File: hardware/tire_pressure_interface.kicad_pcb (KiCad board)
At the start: 4 copper layers, 60.3 x 60.4 mm, 82 parts, among them IC1 TPS54202HDDCR, J3 FTSH-107-01-L-D-K, J4 Conn_02x02_Counter_Clockwise, J5 Micro_SD_Card_Det1, Q1 SI2347DS-T1-GE3, T1 TP_+3V3, T10 TP_+5V, T11 TP_+5V, T3 TP_VCC, T8 TP_VCC, T9 TP_+3V3, U1 STM32G0C1KCTxN, U2 LM1117-3.3, U3 XIAO-ESP32-S3-DIP, U7 ADM3057ExRW

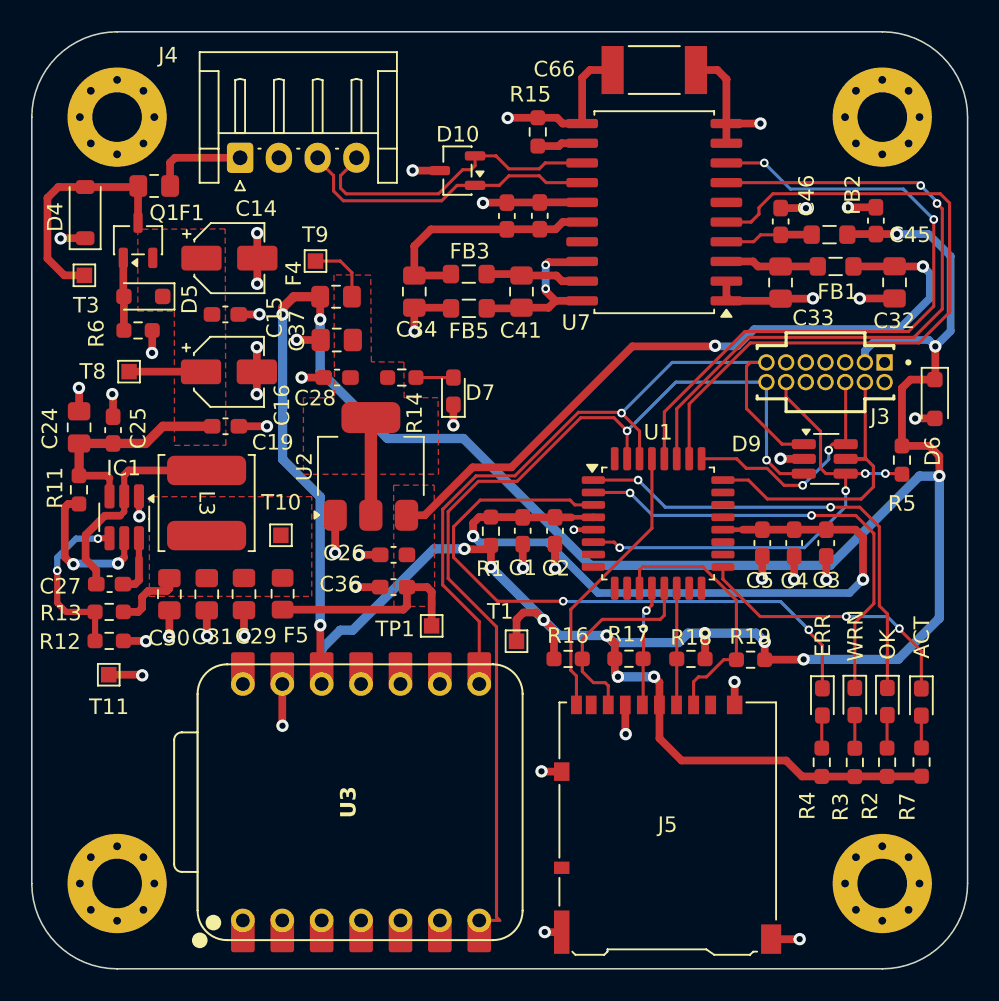
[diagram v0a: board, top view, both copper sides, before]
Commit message: improved 3V3 routing
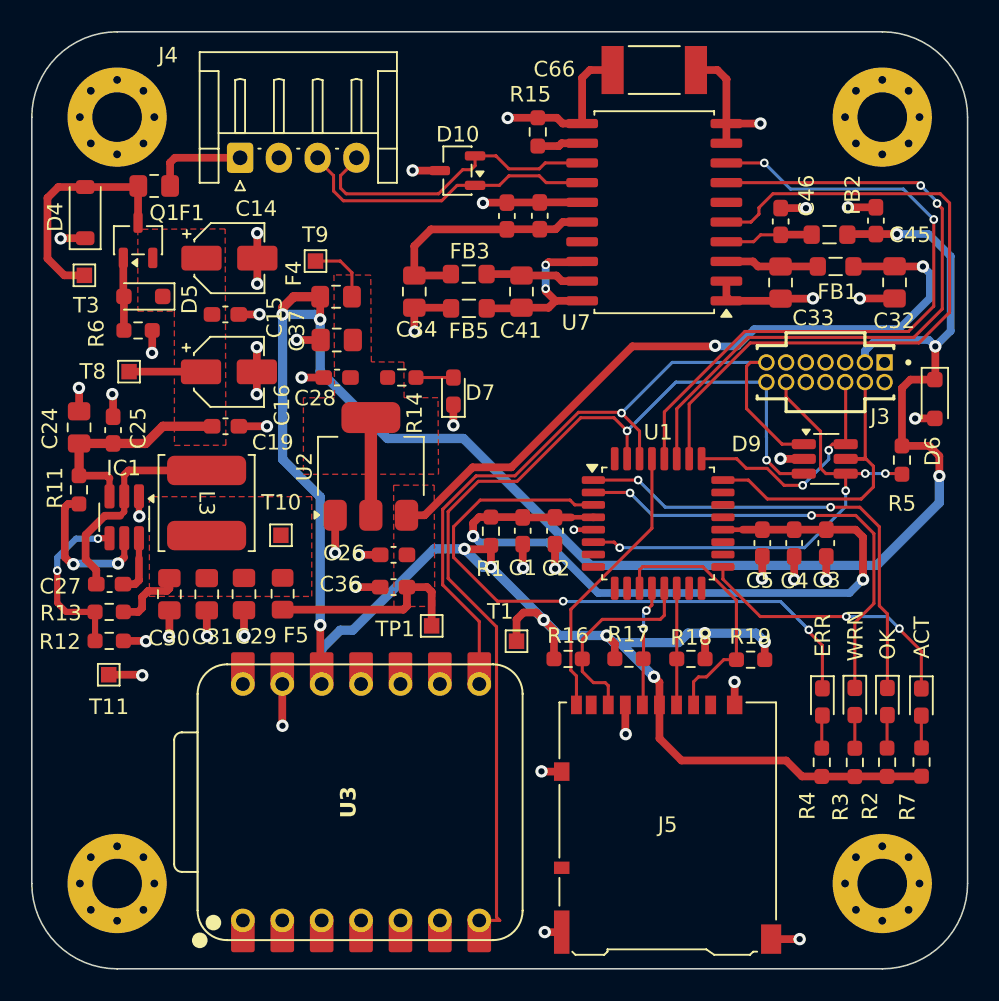
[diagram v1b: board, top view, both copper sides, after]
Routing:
- net +3V3: track 206.6 -> 190.8 mm, vias 15 -> 13
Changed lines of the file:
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@@
 	)
 	(segment
-		(start 117.0625 114.3)
-		(end 119.55 114.3)
-		(width 0.5)
-		(layer "F.Cu")
-		(net "+3V3")
-	)
-	(segment
 		(start 128.06 96.2125)
 		(end 128.03 96.2425)
@@
 	)
 	(segment
-		(start 107.6 115.4)
-		(end 107.3975 115.1975)
-		(width 0.5)
-		(layer "F.Cu")
-		(net "+3V3")
-	)
-	(segment
 		(start 124.23 86.86)
 		(end 125.58 86.86)
@@
 	)
 	(segment
-		(start 107.3975 115.1975)
-		(end 107.3975 114.24)
-		(width 0.5)
-		(layer "F.Cu")
-		(net "+3V3")
-	)
-	(segment
 		(start 88.527634 91.027634)
 		(end 88.4 90.9)
@@
 	)
 	(segment
-		(start 119.55 114.3)
-		(end 119.57 114.28)
-		(width 0.5)
-		(layer "F.Cu")
-		(net "+3V3")
-	)
-	(segment
 		(start 99.41 106.9325)
 		(end 99.41 108.33)
@@
 	)
 	(via
-		(at 119.57 114.28)
-		(size 0.8)
-		(drill 0.4)
-		(layers "F.Cu" "B.Cu")
-		(net "+3V3")
-	)
-	(via
 		(at 109.9225 115.4)
 		(size 0.8)
@@
 	)
 	(via
-		(at 107.6 115.4)
-		(size 0.8)
-		(drill 0.4)
-		(layers "F.Cu" "B.Cu")
-		(net "+3V3")
-	)
-	(via
 		(at 85.98 92.04)
 		(size 0.8)
@@
 	)
 	(segment
-		(start 112.11 112.59)
-		(end 113.2 112.59)
+		(start 85.98 92.04)
+		(end 88.077747 92.04)
 		(width 0.6)
 		(layer "B.Cu")
@@
 	)
 	(segment
-		(start 111.5 113.2)
-		(end 112.11 112.59)
+		(start 112.11 112.59)
+		(end 113.2 112.59)
 		(width 0.6)
 		(layer "B.Cu")
@@
 	)
 	(segment
-		(start 95.741507 107.158493)
-		(end 90.5 112.4)
+		(start 111.5 113.2)
+		(end 112.11 112.59)
 		(width 0.6)
 		(layer "B.Cu")
@@
 	)
 	(segment
-		(start 92.74 100.04)
-		(end 88.4 95.7)
+		(start 107.7225 113.2)
+		(end 109.9225 115.4)
 		(width 0.6)
 		(layer "B.Cu")
@@
 	)
 	(segment
-		(start 119.57 114.28)
-		(end 125.66 114.28)
+		(start 98.871507 108.33)
+		(end 99.41 108.33)
 		(width 0.6)
 		(layer "B.Cu")
@@
 	)
 	(segment
-		(start 125.66 114.28)
-		(end 128.32 111.62)
+		(start 95.741507 107.158493)
+		(end 90.5 112.4)
 		(width 0.6)
 		(layer "B.Cu")
@@
 	)
 	(segment
-		(start 106.87 112.74)
-		(end 107.33 113.2)
+		(start 128.32 104.18)
+		(end 128.32 102.46)
 		(width 0.6)
 		(layer "B.Cu")
@@
 	)
 	(segment
-		(start 97.64 100.04)
-		(end 92.74 100.04)
+		(start 106.87 112.74)
+		(end 107.33 113.2)
 		(width 0.6)
 		(layer "B.Cu")
@@
 	)
 	(segment
+		(start 124.28 108.22)
+		(end 128.32 104.18)
+		(width 0.6)
+		(layer "B.Cu")
+		(net "+3V3")
+	)
+	(segment
 		(start 103.81 112.74)
 		(end 102.81 111.74)
@@
 	)
 	(segment
-		(start 105.82 108.22)
-		(end 97.64 100.04)
+		(start 97.64 100.04)
+		(end 105.82 108.22)
+		(width 0.6)
+		(layer "B.Cu")
+		(net "+3V3")
+	)
+	(segment
+		(start 107.33 113.2)
+		(end 107.7225 113.2)
 		(width 0.6)
 		(layer "B.Cu")
@@
 	)
 	(segment
-		(start 88.4 95.7)
-		(end 88.4 92.367747)
+		(start 92.74 100.04)
+		(end 97.64 100.04)
+		(width 0.6)
+		(layer "B.Cu")
+		(net "+3V3")
+	)
+	(segment
+		(start 97.7 107.158493)
+		(end 98.871507 108.33)
 		(width 0.6)
 		(layer "B.Cu")
@@
 	)
 	(segment
-		(start 128.32 102.46)
-		(end 127.04 102.46)
+		(start 88.4 92.367747)
+		(end 88.4 95.7)
 		(width 0.6)
 		(layer "B.Cu")
@@
 	)
 	(segment
-		(start 128.32 111.62)
-		(end 128.32 102.46)
+		(start 105.82 108.22)
+		(end 124.28 108.22)
 		(width 0.6)
 		(layer "B.Cu")
@@
 	)
 	(segment
-		(start 123.52 95.135)
-		(end 123.52 94.385467)
-		(width 0.5)
-		(layer "B.Cu")
-		(net "+3V3")
-	)
-	(segment
-		(start 121.28 108.22)
-		(end 105.82 108.22)
+		(start 88.4 95.7)
+		(end 92.74 100.04)
 		(width 0.6)
 		(layer "B.Cu")
@@
 	)
 	(segment
-		(start 107.6 115.4)
-		(end 109.9225 115.4)
-		(width 0.6)
+		(start 123.52 95.135)
+		(end 123.52 94.385467)
+		(width 0.5)
 		(layer "B.Cu")
 		(net "+3V3")
@@
 	)
 	(segment
+		(start 88.077747 92.04)
+		(end 88.402747 92.365)
+		(width 0.6)
+		(layer "B.Cu")
+		(net "+3V3")
+	)
+	(segment
 		(start 127.62 86.86)
 		(end 125.58 86.86)
@@
 	)
 	(segment
-		(start 127.04 102.46)
-		(end 121.28 108.22)
-		(width 0.6)
-		(layer "B.Cu")
-		(net "+3V3")
-	)
-	(segment
 		(start 90.5 112.4)
 		(end 89.7 112.4)
@@
 	(group ""
 		(members "00703dba-4c2e-42fc-a1a8-cf139ca52dc6" "05a62035-da1d-40f0-97ea-851d3fd80436"
+			"05b87eb7-f377-4768-b86c-c9f7ca0d2276" "095c8aed-fcb7-42a8-a8f0-d90fc4b4ae68"
 			"0d5e857f-533f-4467-bf6d-914327566aba" "0fa4c703-9df0-4ab2-8ef0-5c3edb20d0ad"
 			"1208581f-ff39-416c-adbe-a18ec6e0bf28" "14e6360a-6a4b-4444-8b3c-591376e39133"
@@
 			"4e00eb45-84cb-4b3e-8a0c-8177cd94ae54" "4e1a9b11-96ea-4c99-8b99-951dbc3321bf"
 			"5459ac72-f4ad-46ea-b973-221839fc366c" "590df0a4-c60b-465d-92d2-229a5f239f01"
-			"603a99ce-778c-4cc2-ac47-9dd50f663a1e" "61661fc5-8242-4758-bd57-87675214378d"
-			"6201897d-be50-4ea8-b066-81e145071469" "685f5b81-1960-4ece-8c2f-54375cb158e5"
-			"721e5f93-0e1b-4f20-94fb-5de0d11acf88" "73bdc88d-e83c-4761-8aba-2511e72a2e7b"
-			"762d14e7-1055-4f50-b1ff-c2fcde72f1f8" "7cd310ce-5e99-443f-b037-ae63036c30b2"
-			"85586006-e9f4-4c2f-8508-362ee8b3d07e" "86e373ea-a50c-4cc0-aff3-3a68b4472e18"
-			"8fe922f6-f549-4147-b541-f0e2f1939003" "928cc488-62c2-467b-b473-730bea197279"
-			"9ed68370-d114-43b4-bf8d-adec00a0048b" "a3589b84-0a47-460b-8f78-c3393f230d29"
-			"a6948ade-f553-4958-9956-c073d8a6550c" "aa374f94-2b74-4cbe-9679-c93f8764b395"
+			"5ac6def6-47a8-4de7-b5ac-e56a859d3408" "603a99ce-778c-4cc2-ac47-9dd50f663a1e"
+			"61661fc5-8242-4758-bd57-87675214378d" "6201897d-be50-4ea8-b066-81e145071469"
+			"685f5b81-1960-4ece-8c2f-54375cb158e5" "721e5f93-0e1b-4f20-94fb-5de0d11acf88"
+			"73bdc88d-e83c-4761-8aba-2511e72a2e7b" "762d14e7-1055-4f50-b1ff-c2fcde72f1f8"
+			"7cd310ce-5e99-443f-b037-ae63036c30b2" "85586006-e9f4-4c2f-8508-362ee8b3d07e"
+			"86e373ea-a50c-4cc0-aff3-3a68b4472e18" "8fe922f6-f549-4147-b541-f0e2f1939003"
+			"928cc488-62c2-467b-b473-730bea197279" "9ed68370-d114-43b4-bf8d-adec00a0048b"
+			"a3589b84-0a47-460b-8f78-c3393f230d29" "aa374f94-2b74-4cbe-9679-c93f8764b395"
 			"adc405e1-fe45-442f-9b69-494e0f701753" "b075e7b7-5082-4849-9a16-9e1e9daf6310"
 			"b0d77d62-8b8b-43d8-976e-da9230c87e7a" "b3e6abc9-8a6f-4ef6-9a0c-72aa0e9f2d1e"
-			"bbb3ab41-f5a9-494c-9cc5-d73b4948d41b" "bdd3e4f7-5517-423c-b4c3-fccdbbc86c31"
-			"c61f7862-0374-402d-9232-37e87592f53d" "c9a31d40-cdae-4f9f-8463-8cf9fbdc15d2"
+			"bdd3e4f7-5517-423c-b4c3-fccdbbc86c31" "c61f7862-0374-402d-9232-37e87592f53d"
 			"ca4472db-32c5-4f6d-a198-702e68f0ebab" "caaab360-6ac4-4656-a9bd-76d31c0d3772"
 			"cd769815-78c4-4f61-9006-5153e65c1106" "d044e153-045c-400b-a4ca-aff362360da5"
-			"d989c95a-8158-4790-b372-f06467a94cc8" "dc01cbed-65fb-4b73-95b4-78ab054667fe"
-			"e1a60196-51ce-4d69-a6e7-8c5a97a9d763" "e4d6bcbe-3935-463d-a843-e06c1e6375a7"
-			"e546ec76-b08e-4dc9-acde-533788c9ce6c" "ebe58213-7ecb-40e2-b4dd-223eeca81cea"
-			"eefec69f-36b7-4e23-8b1f-b1cc1d064f99" "ef02022c-a614-4320-976d-3db820095535"
+			"d682385c-291b-499c-a74b-18475480bd1b" "d989c95a-8158-4790-b372-f06467a94cc8"
+			"dc01cbed-65fb-4b73-95b4-78ab054667fe" "e1a60196-51ce-4d69-a6e7-8c5a97a9d763"
+			"e4d6bcbe-3935-463d-a843-e06c1e6375a7" "e546ec76-b08e-4dc9-acde-533788c9ce6c"
+			"ebe58213-7ecb-40e2-b4dd-223eeca81cea" "eefec69f-36b7-4e23-8b1f-b1cc1d064f99"
 			"efd51114-acd2-4af0-97d3-ae698a8f72a2" "f322b5dc-610d-4977-9d25-ae899c84eb65"
 			"f3ff9a4a-9da2-4b16-9a4e-7581b2c3153a" "f496a49a-3701-426a-932a-ab3e8247cca4"

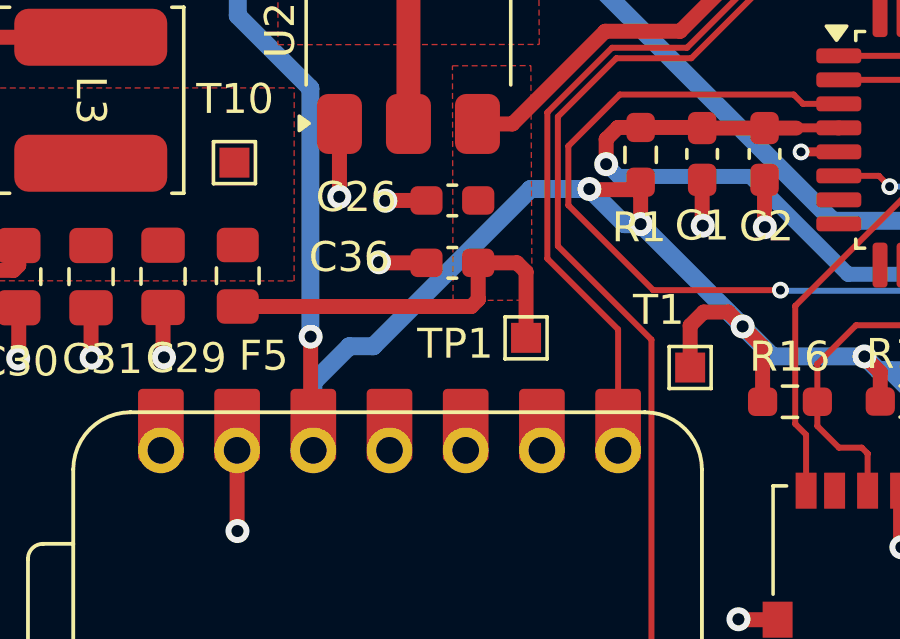
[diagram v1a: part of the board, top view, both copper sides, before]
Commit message: fixed 3v3 routing
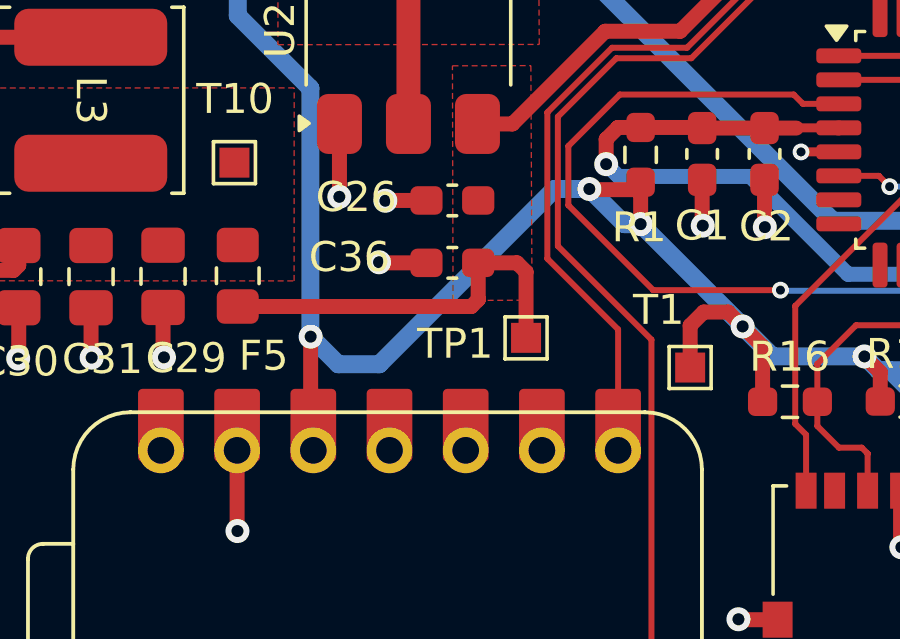
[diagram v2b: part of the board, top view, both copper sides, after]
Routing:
- net +3V3: track 190.8 -> 188.8 mm
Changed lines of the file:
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@@
+	)
+	(segment
+		(start 90.7 113)
+		(end 96.541507 107.158493)
+		(width 0.6)
+		(layer "B.Cu")
+		(net "+3V3")
 	)
 	(segment
@@
 	)
 	(segment
-		(start 95.741507 107.158493)
-		(end 90.5 112.4)
+		(start 88.41 112.08)
+		(end 89.33 113)
+		(width 0.6)
+		(layer "B.Cu")
+		(net "+3V3")
+	)
+	(segment
+		(start 89.33 113)
+		(end 90.7 113)
 		(width 0.6)
 		(layer "B.Cu")
@@
 	)
 	(segment
-		(start 97.7 107.158493)
-		(end 95.741507 107.158493)
-		(width 0.6)
-		(layer "B.Cu")
-		(net "+3V3")
-	)
-	(segment
 		(start 128.32 104.18)
 		(end 128.32 102.46)
@@
 	)
 	(segment
-		(start 88.4985 113.6015)
-		(end 88.4985 115.87)
-		(width 0.6)
-		(layer "B.Cu")
-		(net "+3V3")
-	)
-	(segment
 		(start 97.64 100.04)
 		(end 105.82 108.22)
@@
 	)
 	(segment
-		(start 89.7 112.4)
-		(end 88.4985 113.6015)
-		(width 0.6)
-		(layer "B.Cu")
-		(net "+3V3")
-	)
-	(segment
 		(start 102.81 111.74)
 		(end 102.81 111.73)
@@
 	)
 	(segment
+		(start 96.541507 107.158493)
+		(end 97.7 107.158493)
+		(width 0.6)
+		(layer "B.Cu")
+		(net "+3V3")
+	)
+	(segment
 		(start 127.62 86.86)
 		(end 125.58 86.86)
@@
 		(layer "B.Cu")
 		(net "+3V3")
-	)
-	(segment
-		(start 90.5 112.4)
-		(end 89.7 112.4)
-		(width 0.6)
-		(layer "B.Cu")
-		(net "+3V3")
